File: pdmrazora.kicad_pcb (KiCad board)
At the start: 2 copper layers, 109 x 98 mm, 54 parts, among them J1 6473418-1, J2 M6_VBAT, J3 M6_GND, M1000 Module:mega-mcu144/0.7, U1 BTS50010-1TAD, U11 BTS7004-1EPP, U12 BTS7004-1EPP, U13 BTS7004-1EPP, U14 BTS7004-1EPP, U15 BTS7004-1EPP, U16 BTS7004-1EPP, U17 BTS7004-1EPP, U18 BTS7004-1EPP, U2 BTS50010-1TAD, U3 BTS50010-1TAD, U4 BTS50010-1TAD

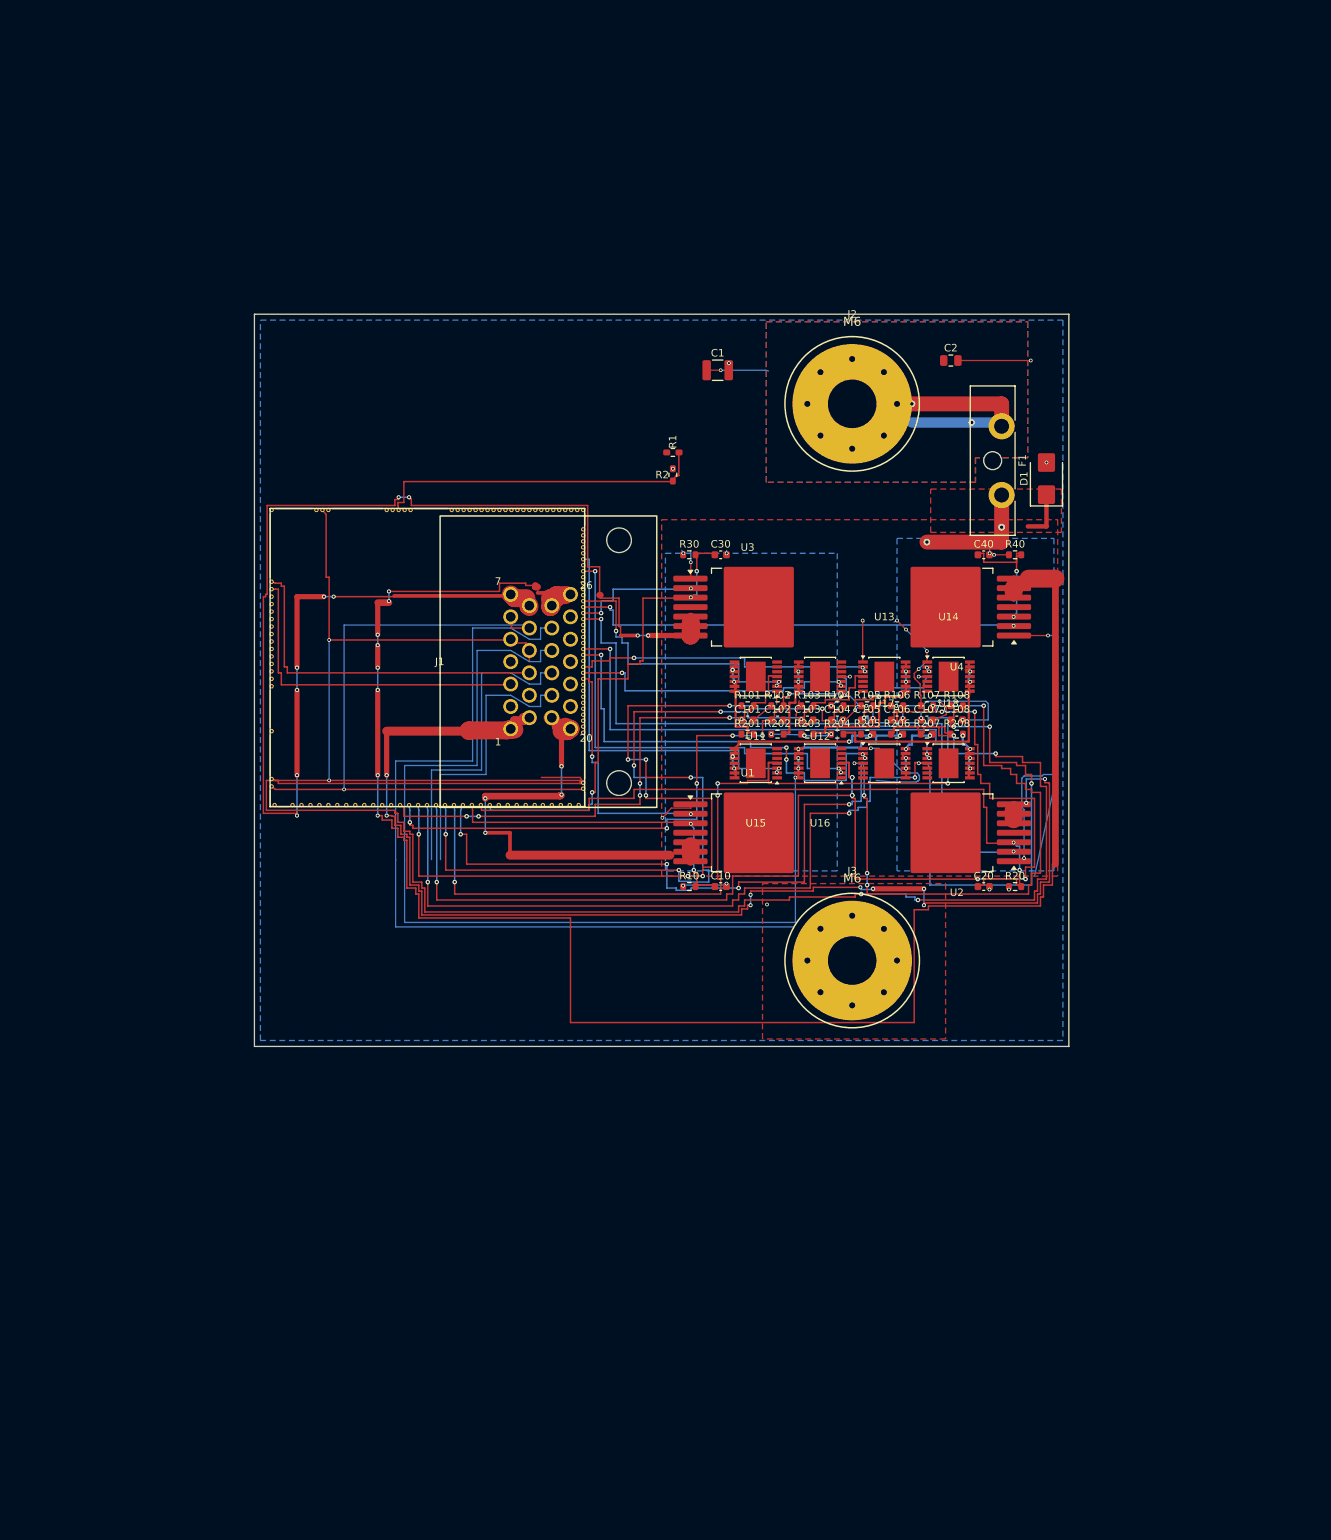
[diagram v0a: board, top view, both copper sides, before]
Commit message: Grow the outline to 174x202 mm and pour HP channels at the 1 oz width.
PWR_OUT1–4 now have continuous pour necks at the IPC-2221A 16.72 mm line. J1, J3, and F1 stay put; M1000 and the west drivers move only enough to open the corridors.

Co-authored-by: Quintin <quintinbannink42@users.noreply.github.com>
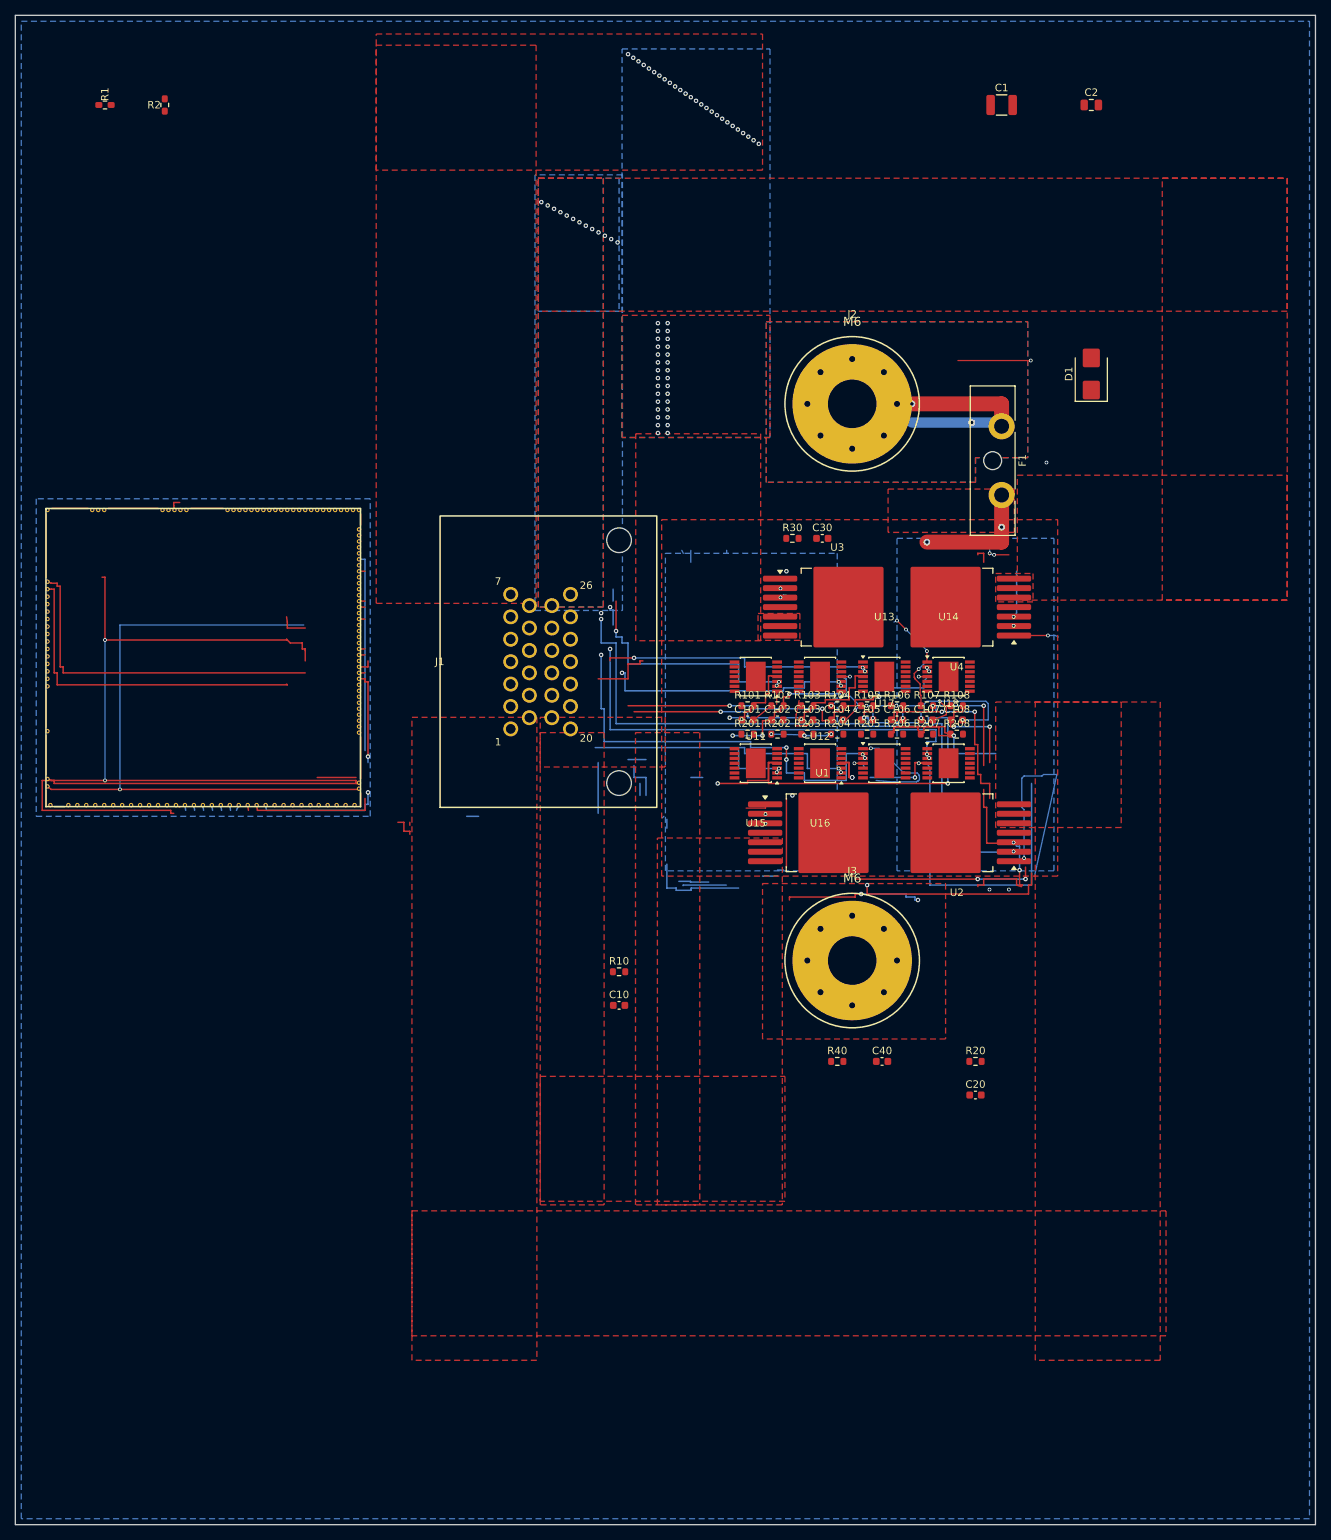
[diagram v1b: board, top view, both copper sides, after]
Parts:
- moved R1 89.1 mm to (-20.0, -28.0)
- moved R2 84.1 mm to (-12.0, -28.0)
- moved R40 71.9 mm to (78.0, 100.0)
- moved C40 69.2 mm to (84.0, 100.0)
- moved C1 52.0 mm to (100.0, -28.0)
- moved C2 39.0 mm to (112.0, -28.0)
- moved M1000 30.0 mm to (-28.0, 66.0)
- moved C20 27.9 mm to (96.5, 104.5)
- moved R20 24.0 mm to (96.5, 100.0)
- moved C10 20.9 mm to (48.8, 92.5)
- moved D1 15.2 mm to (112.0, 8.00)
- moved R10 14.8 mm to (48.8, 88.0)
- moved R30 14.0 mm to (72.0, 30.0)
- moved C30 13.8 mm to (76.0, 30.0)
- moved U3 12.0 mm to (78.0, 39.2)
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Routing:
- net PWR_OUT4: track 247.2 -> 0.00 mm, vias 8 -> 13
- net PWR_OUT3: track 188.0 -> 0.00 mm, vias 10 -> 56
- net PWR_OUT2: track 168.2 -> 0.00 mm, vias 10 -> 0
- net ADIO6: track 151.7 -> 0.00 mm, vias 5 -> 0
- net ADIO8: track 124.7 -> 0.00 mm, vias 4 -> 0
- net SENSOR_5V: track 348.1 -> 230.5 mm, vias 9 -> 8
- net IN_RES1: track 176.6 -> 62.2 mm, vias 9 -> 6
- net IN_RES2: track 173.9 -> 66.7 mm, vias 11 -> 5
- net IN_RES3: track 168.5 -> 70.9 mm, vias 7 -> 4
- net ADIO4: track 74.1 -> 0.00 mm, vias 2 -> 0
- net IN_O2S: track 130.0 -> 59.7 mm, vias 9 -> 4
- net IN_MAP3: track 118.8 -> 55.2 mm, vias 7 -> 2
- net IN_O2S2: track 127.5 -> 65.5 mm, vias 5 -> 4
- net PWR_OUT1: track 59.5 -> 0.00 mm, vias 4 -> 0
- net OUT_PWM4: track 60.3 -> 3.88 mm
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- added copper zone on F.Cu, net PWR_OUT1
- added copper zone on F.Cu, net PWR_OUT2
- added copper zone on B.Cu, net PWR_OUT3
- added copper zone on F.Cu, net PWR_OUT3
- added copper zone on B.Cu, net PWR_OUT4
- added copper zone on F.Cu, net PWR_OUT4
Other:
- board size 109 x 98 mm -> 174 x 202 mm

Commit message: Pour the odd ADIO channels at the 1 oz 8 A width.
ADIO1, ADIO3, ADIO5, and ADIO7 leave J1 on F+B, or on a 3.80 mm B.Cu leg, and the series neck meets 3.47 mm. The even SuperSeal pins stay open because the pin-field aperture is 0.60 mm. HP pours are unchanged.

Co-authored-by: Quintin <quintinbannink42@users.noreply.github.com>
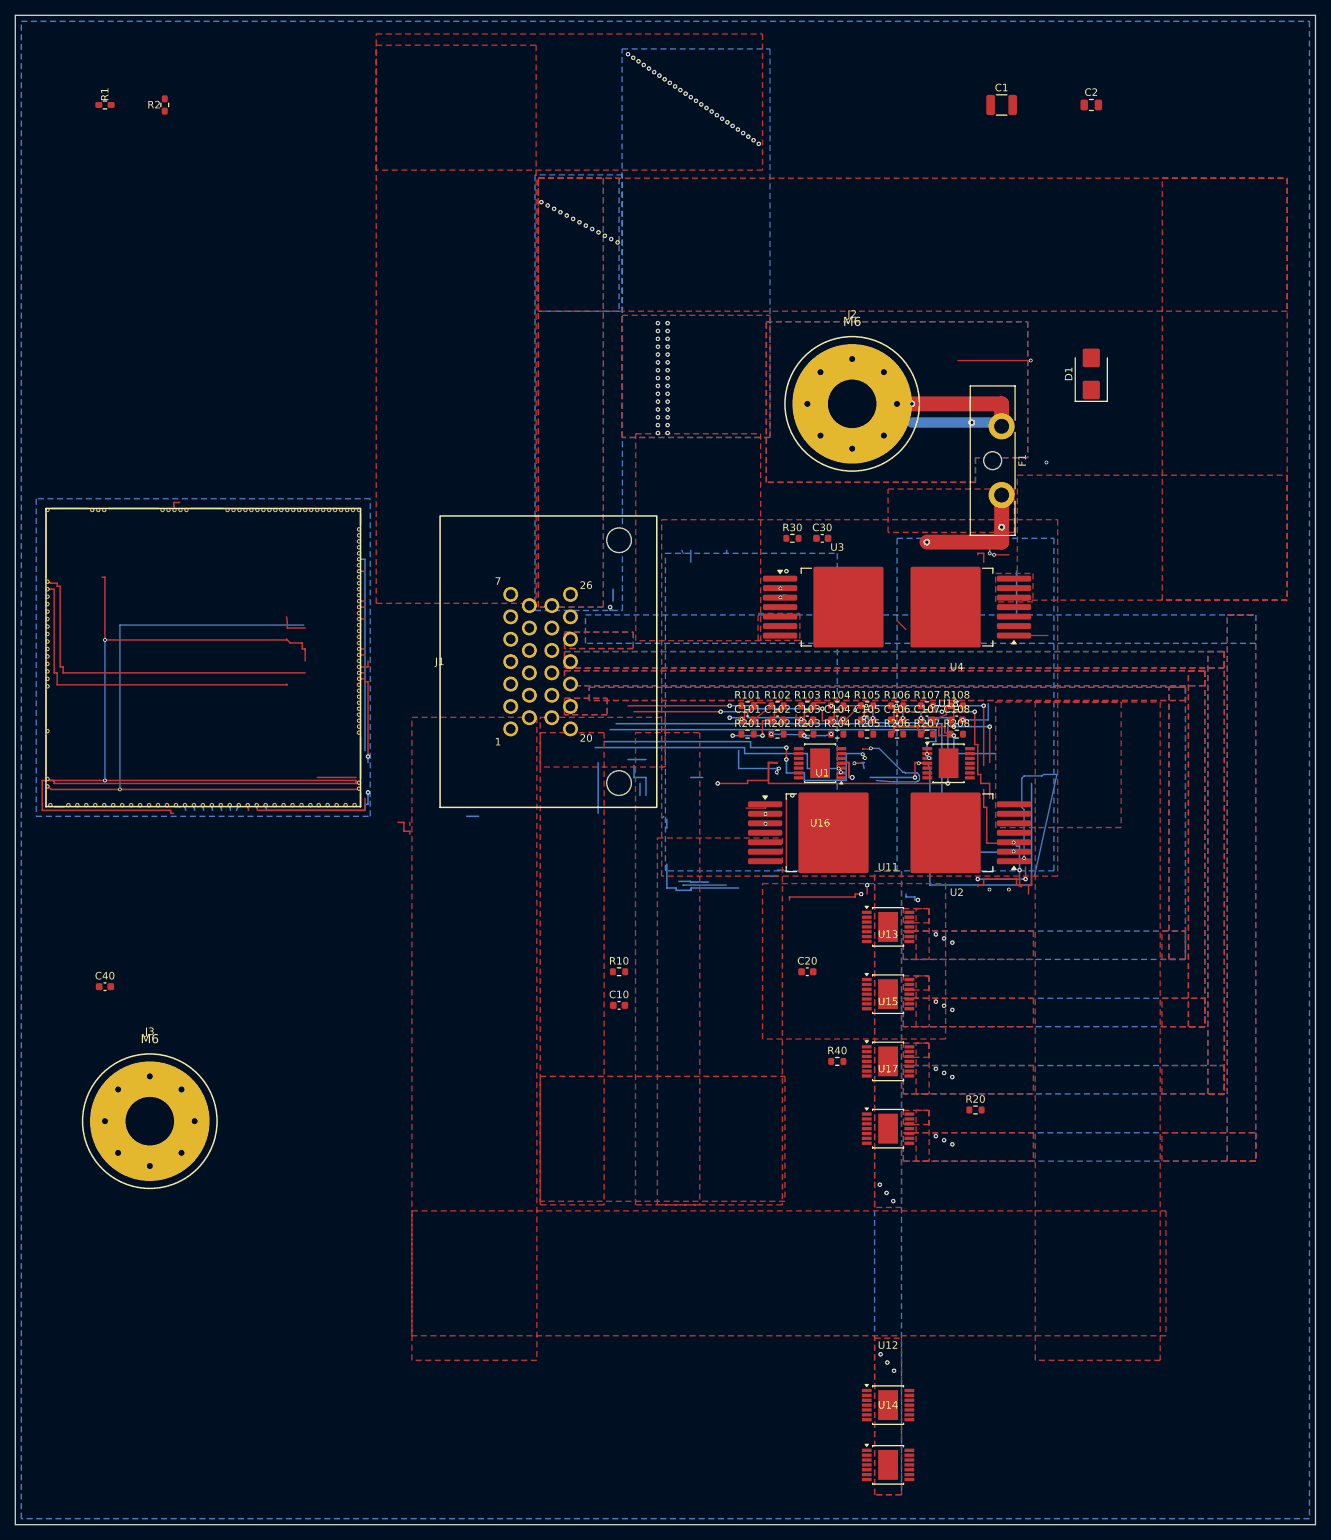
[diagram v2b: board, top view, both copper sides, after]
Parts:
- moved U14 105.8 mm to (84.8, 154.0)
- moved C40 104.5 mm to (-20.0, 90.0)
- moved U12 97.9 mm to (84.8, 146.0), turned to 0 degrees
- moved J3 96.4 mm to (-14.0, 108.0)
- moved U17 48.9 mm to (84.8, 109.0)
- moved U15 43.6 mm to (84.8, 100.0), turned to 0 degrees
- moved U13 42.5 mm to (84.8, 91.0)
- moved U11 37.9 mm to (84.8, 82.0), turned to 0 degrees
- moved C20 27.9 mm to (74.0, 88.0)
- moved R20 6.50 mm to (96.5, 106.5)
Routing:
- net OUT_PWM7: track 39.2 -> 2.00 mm, vias 3 -> 0
- net OUT_PWM6: track 35.6 -> 0.80 mm, vias 3 -> 0
- net OUT_PWM5: track 34.9 -> 0.80 mm, vias 3 -> 0
- net GND: track 145.7 -> 112.5 mm, vias 23 -> 16
- net IN_RES2: track 66.7 -> 45.1 mm
- net IN_RES1: track 62.2 -> 45.8 mm
- net OUT_PWM2: track 88.1 -> 72.1 mm, vias 2 -> 1
- net IN_O2S: track 59.7 -> 44.2 mm, vias 4 -> 2
- net IN_MAP2: track 28.2 -> 13.1 mm, vias 4 -> 2
- net OUT_IO7: track 58.0 -> 46.0 mm, vias 5 -> 4
- net OUT_IO8: track 61.2 -> 50.4 mm, vias 3 -> 2
- net IN_MAP3: track 55.2 -> 46.6 mm
- net IN_AUX3: track 26.3 -> 17.9 mm
- net SENSOR_5V: track 230.5 -> 224.5 mm
- net IN_MAP1: track 16.4 -> 11.2 mm
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- added copper zone on B.Cu, net ADIO1
- added copper zone on F.Cu, net ADIO1
- added copper zone on B.Cu, net ADIO3
- added copper zone on F.Cu, net ADIO3
- added copper zone on B.Cu, net ADIO5
- added copper zone on F.Cu, net ADIO5
- added copper zone on B.Cu, net ADIO7
- added copper zone on F.Cu, net ADIO7

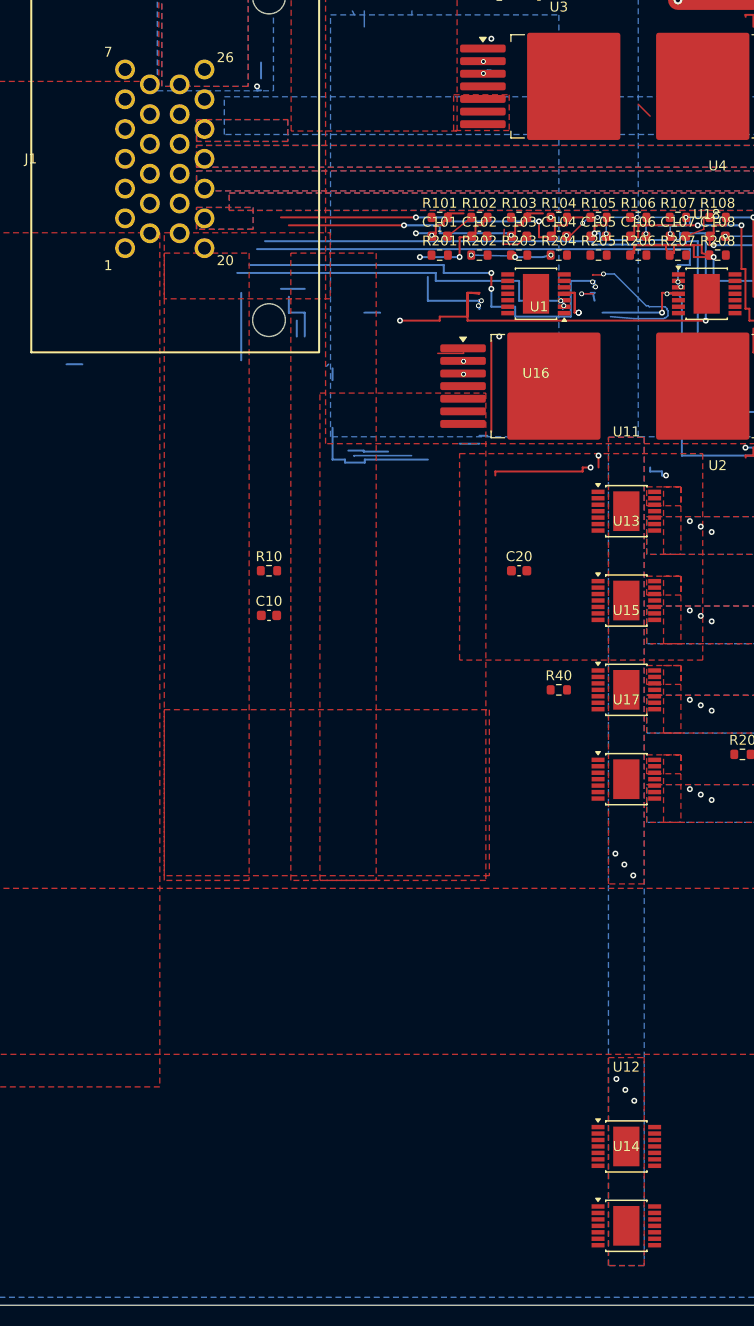
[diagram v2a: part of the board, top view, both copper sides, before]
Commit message: Pour ADIO2 at 4.53 mm through SuperSeal NC pins 2 and 9.
Same-net copper on the unused pads opens one even channel above the
1 oz 8 A line. ADIO4, ADIO6, and ADIO8 stay short of 3.47 mm; pin 25
stays N/C. Hard DRC stays 0.

Co-authored-by: Quintin <quintinbannink42@users.noreply.github.com>
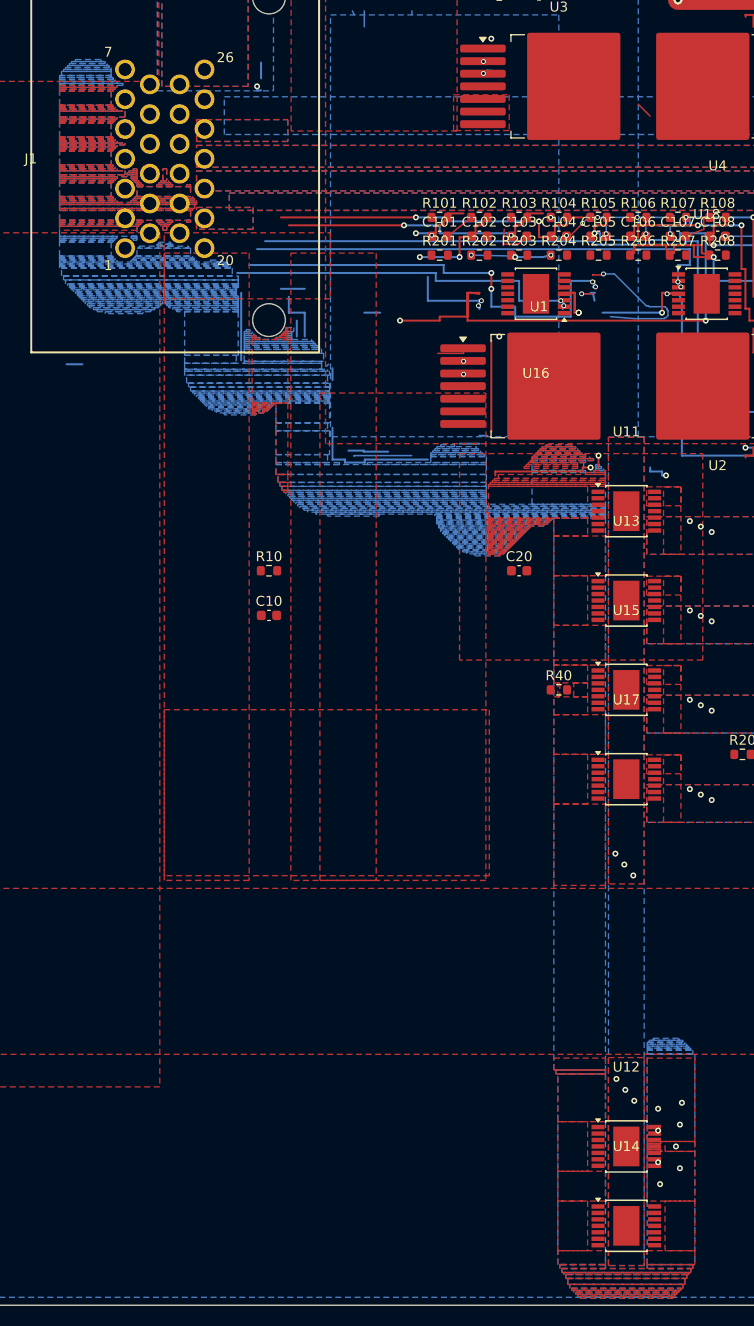
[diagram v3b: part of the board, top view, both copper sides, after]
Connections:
- J1 pad 2: (no net) -> ADIO2
- J1 pad 9: (no net) -> ADIO2
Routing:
- net ADIO2: vias 0 -> 8
- added copper zone on B.Cu, net ADIO2
- added copper zone on F.Cu, net ADIO2
